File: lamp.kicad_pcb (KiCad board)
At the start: 2 copper layers, 24 x 24 mm, 39 parts, among them J101 Conn_01x01_Female, J102 Conn_01x01_Female, J103 Conn_01x01_Female, J104 Conn_01x01_Female, J105 Conn_01x01_Female, J106 Conn_01x01_Female, J107 Conn_01x01_Female, U101 STM32F030F4Px, U102 MIC5205-3.3, U103 TPS54620, U104 LMV321

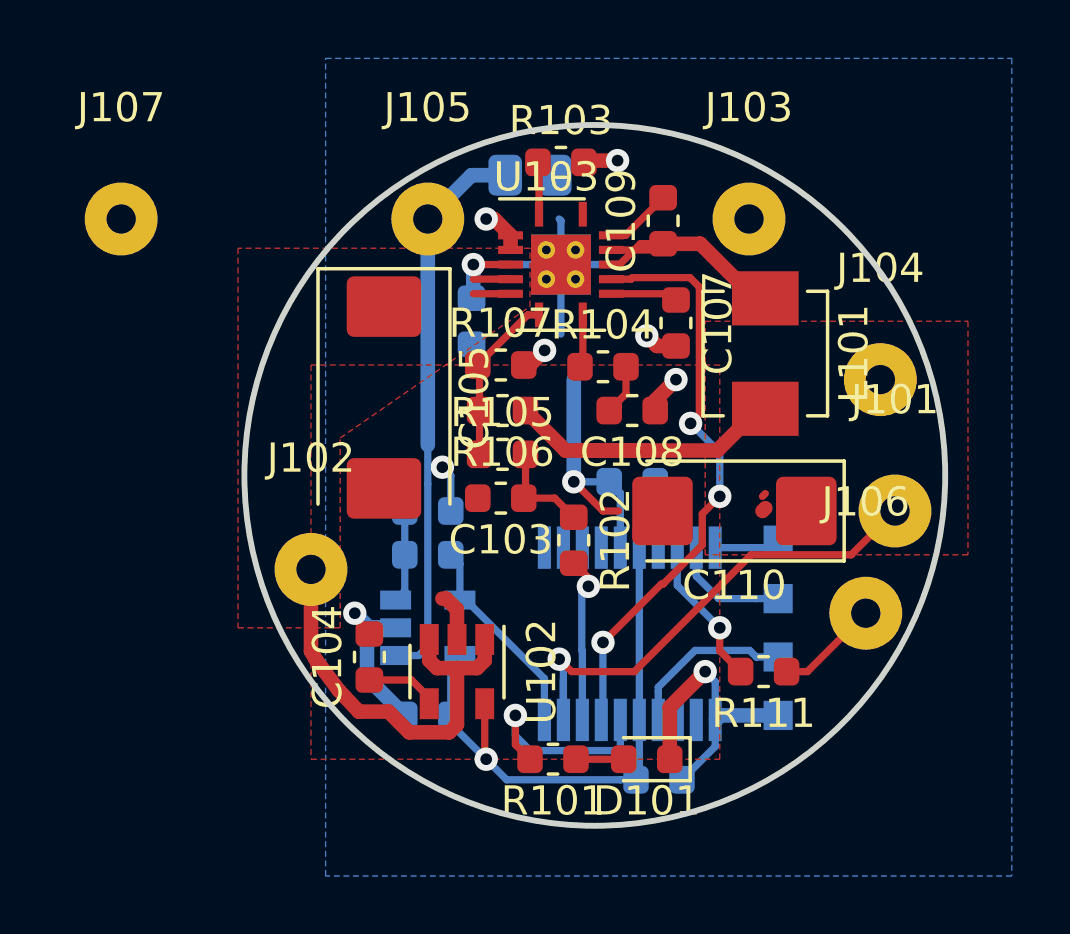
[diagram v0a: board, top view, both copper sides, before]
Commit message: Move to four layers, value selection
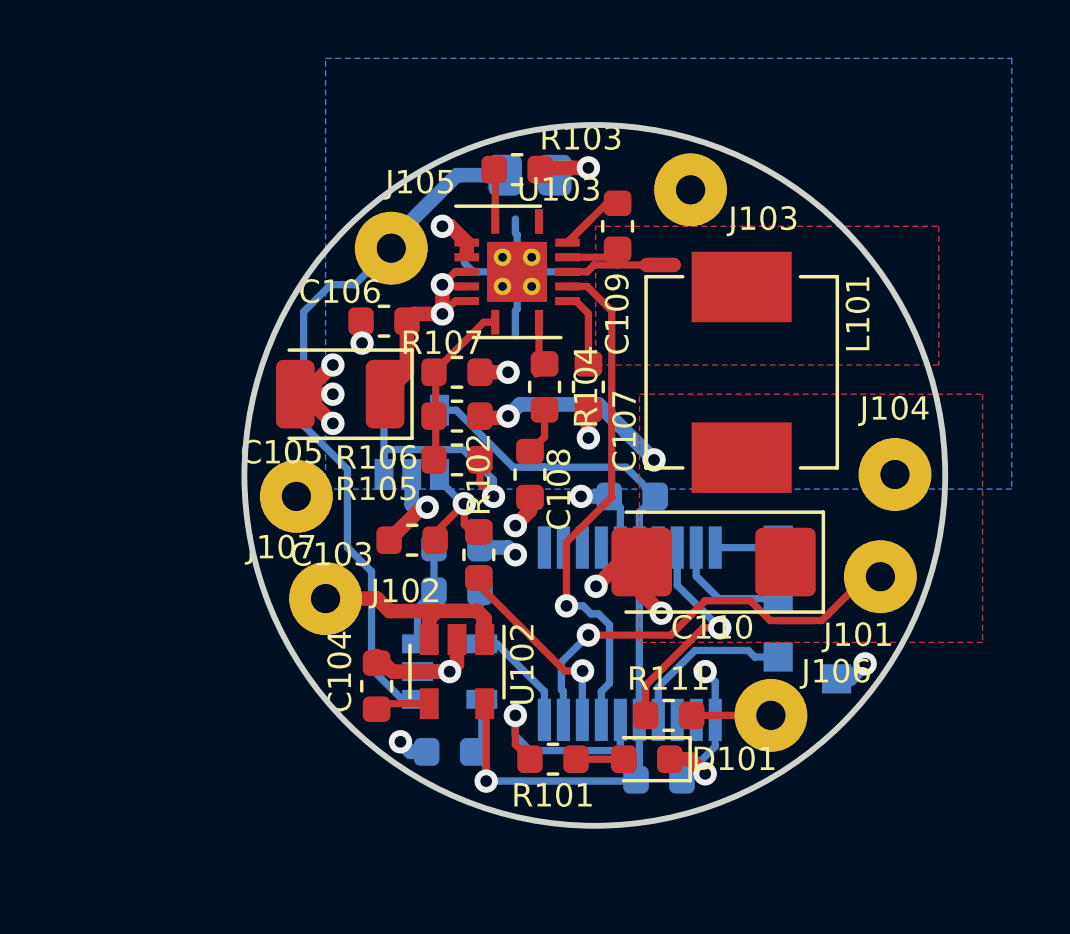
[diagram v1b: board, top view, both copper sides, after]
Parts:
- added U105: LMV321, Package_TO_SOT_SMD:SOT-23-5, B.Cu at (129.4, 82.7)
- C105: footprint Capacitor_Tantalum_SMD:CP_EIA-7343-31_Kemet-D -> Capacitor_Tantalum_SMD:CP_EIA-3528-12_Kemet-T
- C106: moved to F.Cu
- L101: value 3.3u -> 4.7u; footprint Inductor_SMD:L_Vishay_IHLP-1616 -> Inductor_SMD:L_Vishay_IHLP-2525
- R103: value R -> 40k
- R105: value R -> 50k
- R106: value R -> 22k
- R107: value R -> 4.7k
- moved J107 11.2 mm to (125.5, 84.5)
- moved J106 4.78 mm to (141.8, 92.0)
- moved C108 4.13 mm to (133.5, 83.8), turned to 90 degrees
- moved C107 3.71 mm to (135.5, 80.8)
- moved R111 3.58 mm to (138.2, 92.0)
- moved C103 3.36 mm to (129.5, 86.0)
- moved J104 3.29 mm to (146.0, 83.8)
- moved R102 3.29 mm to (131.8, 86.5)
- moved C106 3.00 mm to (128.5, 78.5), turned to 180 degrees
- moved TP104 2.36 mm to (144.0, 90.8)
- moved J101 2.30 mm to (145.5, 87.2)
- moved J103 2.24 mm to (139.0, 74.0)
- moved R104 2.12 mm to (134.0, 80.8), turned to 270 degrees
- moved C110 1.89 mm to (139.8, 86.8)
- moved U104 1.68 mm to (130.8, 90.5)
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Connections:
- R105 pad 2: /SETPOINT -> Net-(R105-Pad2)
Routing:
- net Net-(R105-Pad2): track 0.00 -> 9.20 mm, vias 0 -> 1
- net +3V3: track 22.0 -> 30.2 mm
- net /LED_P: track 12.1 -> 6.88 mm, vias 0 -> 2
- net /ISENSE: track 19.1 -> 24.2 mm
- net /VIN: track 20.3 -> 15.8 mm, vias 1 -> 2
- net /LED2: track 5.14 -> 7.73 mm
- net /EN: track 20.2 -> 17.7 mm, vias 3 -> 1
- net /SW: track 8.42 -> 6.38 mm
- net GND: track 42.3 -> 44.0 mm, vias 9 -> 19
- net Net-(C109-Pad2): track 2.31 -> 3.42 mm
- net /SETPOINT: track 3.48 -> 4.51 mm, vias 0 -> 1
- net Net-(R109-Pad2): track 7.10 -> 6.11 mm
- net /BTN: track 17.5 -> 16.5 mm
- net Net-(J106-Pad1): track 3.54 -> 2.71 mm
- net Net-(R102-Pad2): track 5.68 -> 6.45 mm
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- added copper zone on F.Cu, net /SW
- added copper zone on In2.Cu, net /VIN
- added copper zone on In1.Cu, net GND
- removed copper zone on F.Cu, net /VIN
- removed copper zone on F.Cu, net GND
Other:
- copper layers 2 -> 4

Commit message: More iteration
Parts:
- added C112: 100n, Capacitor_SMD:C_0603_1608Metric, B.Cu at (131.8, 86.0)
- added C113: 100n, Capacitor_SMD:C_0603_1608Metric, B.Cu at (133.0, 82.8)
- added C114: 100n, Capacitor_SMD:C_0603_1608Metric, F.Cu at (133.8, 88.8)
- C108: value 8.2n -> 22n
- C110: footprint Capacitor_Tantalum_SMD:CP_EIA-6032-28_Kemet-C -> Capacitor_Tantalum_SMD:CP_EIA-7343-15_Kemet-W
- L101: footprint Inductor_SMD:L_Vishay_IHLP-2525 -> Inductor_SMD:L_7.3x7.3_H4.5
- R104: value 1.8k -> 1k
- moved J102 3.64 mm to (125.5, 84.5)
- moved J107 3.58 mm to (126.2, 88.0)
- moved TP104 2.06 mm to (143.5, 88.8)
- moved R110 1.53 mm to (129.5, 86.7), turned to 270 degrees
- moved TP101 1.27 mm to (141.8, 88.8)
- moved TP102 1.03 mm to (141.8, 87.0)
- moved C109 1.00 mm to (136.5, 74.2)
- moved C108 0.90 mm to (134.2, 83.2), turned to 180 degrees
- moved TP103 0.79 mm to (141.8, 85.2)
- moved R109 0.75 mm to (131.8, 87.8)
- moved C110 0.59 mm to (139.2, 87.0)
- moved L101 0.50 mm to (140.2, 80.2)
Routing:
- net GND: track 44.0 -> 50.5 mm, vias 19 -> 23
- net Net-(R105-Pad2): track 9.20 -> 12.3 mm
- net /BTN: track 16.5 -> 14.0 mm
- net /EN: track 17.7 -> 20.0 mm
- net Net-(C112-Pad1): track 3.83 -> 5.62 mm
- net Net-(C112-Pad2): track 6.11 -> 7.54 mm
- net /LED2: track 7.73 -> 6.34 mm
- net /SETPOINT: track 4.51 -> 5.06 mm
- net /VIN: track 15.8 -> 15.4 mm, vias 2 -> 3
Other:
- board text added: "BTN"
- board text added: "GND"
- board text added: "IND"
- board text added: "OUT+"
- board text added: "OUT-"
- board text added: "VIN"

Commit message: More iteration
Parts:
- removed C101: 100n, Capacitor_SMD:C_0603_1608Metric
- added C1: 100n, Capacitor_SMD:C_0603_1608Metric, B.Cu at (137.8, 94.5)
- added C15: 100n, Capacitor_SMD:C_0603_1608Metric, F.Cu at (137.0, 93.0)
- added C16: 100n, Capacitor_SMD:C_0603_1608Metric, B.Cu at (133.5, 84.5)
- added R1: 90k, Resistor_SMD:R_0603_1608Metric, F.Cu at (134.2, 92.2)
- added R2: 10k, Resistor_SMD:R_0603_1608Metric, F.Cu at (137.0, 91.5)
- moved TP4 12.0 mm to (135.2, 80.0)
- moved R10 1.80 mm to (139.8, 91.0), turned to 90 degrees
- moved R3 1.04 mm to (134.0, 94.5)
- moved D1 1.02 mm to (137.7, 94.5)
- moved J4 0.90 mm to (142.5, 91.5)
- moved J6 0.50 mm to (146.0, 83.2)
- moved TP1 0.50 mm to (141.8, 89.2)
- moved C3 0.29 mm to (129.8, 86.0)
- moved R4 0.25 mm to (132.0, 86.5)
- moved TP2 0.25 mm to (141.8, 87.2)
- renumbered C107 to C10, C113 to C11, C108 to C12, C109 to C13, C110 to C14, C102 to C2, C103 to C3, C114 to C4, C111 to C5, C112 to C6, C104 to C7, C105 to C8, C106 to C9, D101 to D1, J102 to J1, J103 to J2, J101 to J3, J106 to J4, J107 to J5, J104 to J6, J105 to J7, L101 to L1, R111 to R10, R106 to R11, R107 to R12, R108 to R13, R101 to R3, R102 to R4, R109 to R5, R110 to R6, R103 to R7, R104 to R8, R105 to R9, TP101 to TP1, TP102 to TP2, TP103 to TP3, TP104 to TP4, U101 to U1, U104 to U2, U102 to U3, U103 to U4, U105 to U5
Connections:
- U1 pad 14: Net-(U101-Pad14) -> /VBAT
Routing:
- net /VBAT: track 0.00 -> 9.26 mm, vias 0 -> 1
- net GND: track 50.5 -> 58.3 mm, vias 23 -> 25
- net +3V3: track 29.8 -> 35.2 mm
- net /VIN: track 15.4 -> 19.3 mm
- net Net-(R9-Pad2): track 12.3 -> 8.67 mm
- net /EN: track 20.0 -> 17.4 mm, vias 1 -> 2
- net Net-(C16-Pad1): track 7.54 -> 9.21 mm
- net /LED2: track 6.34 -> 4.71 mm
- net /BTN: track 14.0 -> 15.6 mm
- net /SETPOINT: track 5.06 -> 4.05 mm
- net /LED1: track 7.21 -> 7.99 mm
- net Net-(D1-Pad2): track 1.64 -> 2.18 mm
- net /LED_P: track 6.76 -> 7.28 mm, vias 2 -> 0
- added copper zone on F.Cu, net GND

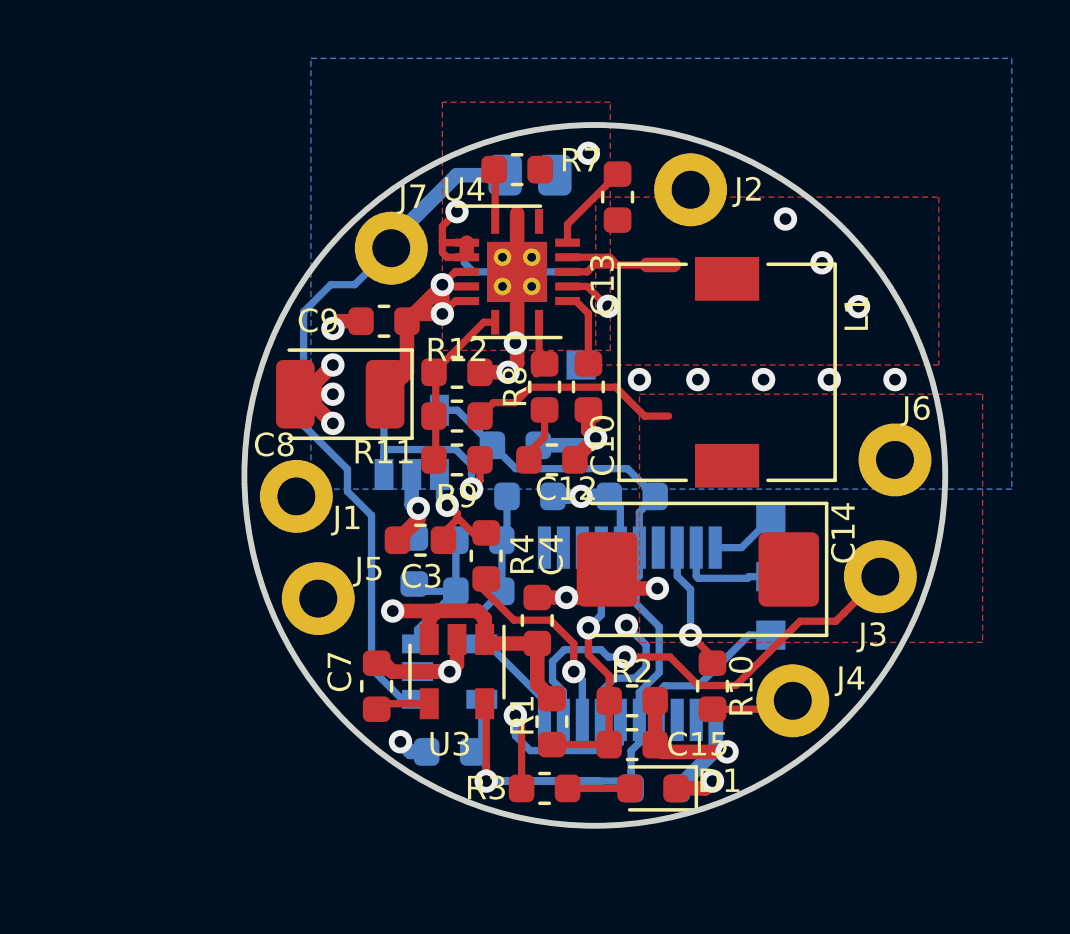
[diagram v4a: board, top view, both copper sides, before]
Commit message: Make LED PWMable
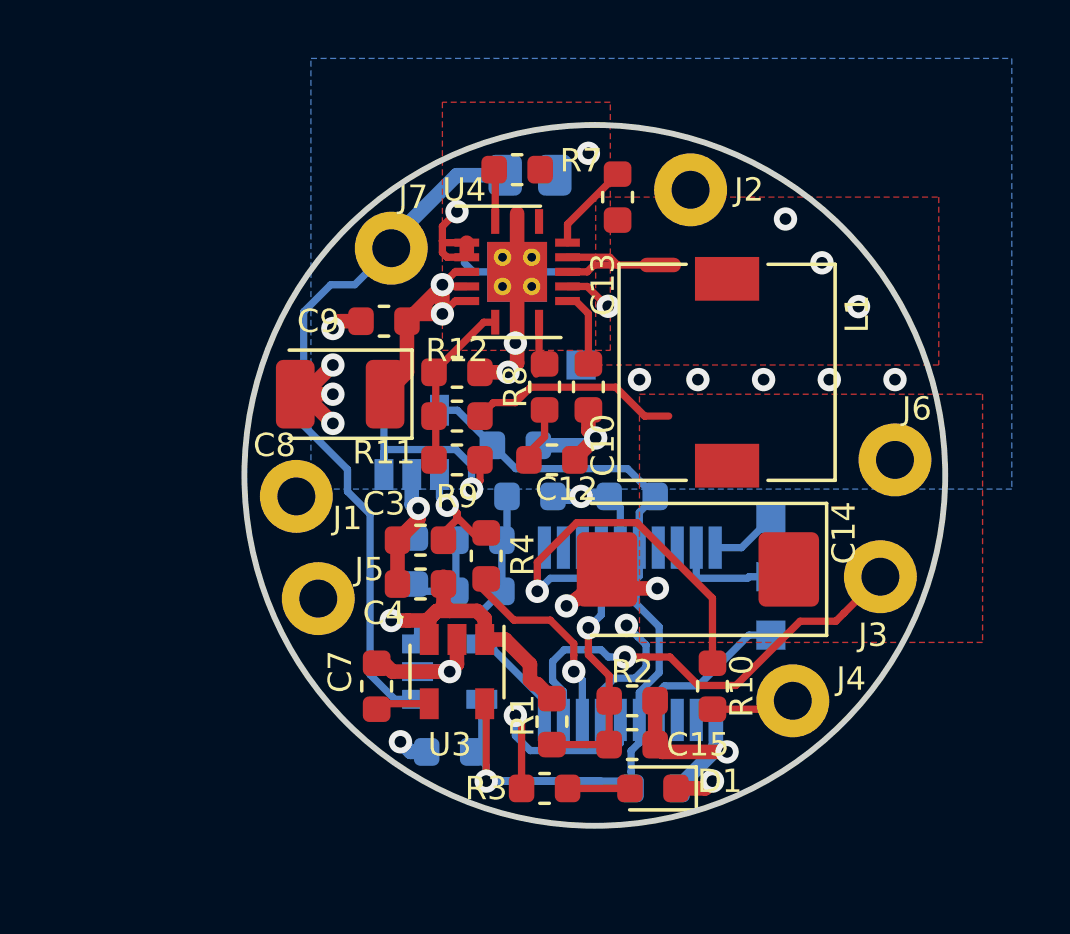
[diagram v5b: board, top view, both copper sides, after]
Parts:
- C15, C16: value 100n -> 10n
- R1: value 90k -> 47k
- R5: value 1k -> 100k
- U1: value STM32F030F4Px -> STM32F030F4P6
- moved C4 4.19 mm to (129.8, 87.5), turned to 180 degrees
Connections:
- U1 pad 13: Net-(U1-Pad13) -> /LED2
- U1 pad 18: /LED2 -> Net-(U1-Pad18)
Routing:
- net /LED2: track 4.71 -> 13.6 mm
- net /VIN: track 19.3 -> 20.2 mm

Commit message: Make other LED PWMable
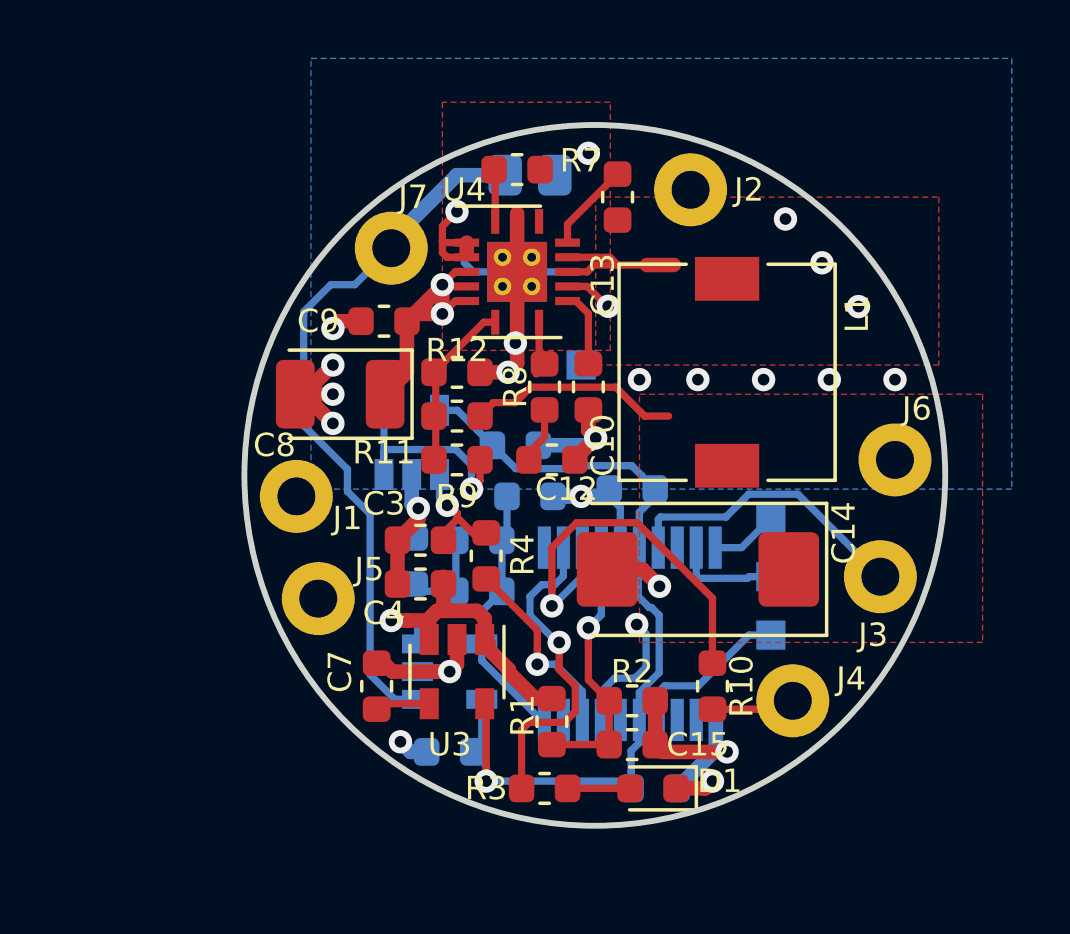
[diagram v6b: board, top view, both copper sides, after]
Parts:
- moved C2 0.25 mm to (137.0, 84.2)
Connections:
- U1 pad 12: Net-(U1-Pad12) -> /LED1
- U1 pad 17: Net-(U1-Pad17) -> /BTN
- U1 pad 6: /LED1 -> Net-(U1-Pad6)
- U1 pad 9: /BTN -> Net-(U1-Pad9)
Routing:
- net /BTN: track 15.6 -> 10.1 mm, vias 1 -> 0
- net +3V3: track 35.2 -> 31.2 mm
- net /LED1: track 7.99 -> 11.1 mm
- net GND: track 58.6 -> 57.6 mm, vias 25 -> 24

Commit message: Wibbles
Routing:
- net GND: track 57.6 -> 59.4 mm, vias 24 -> 25
- net /EN: track 17.4 -> 16.8 mm

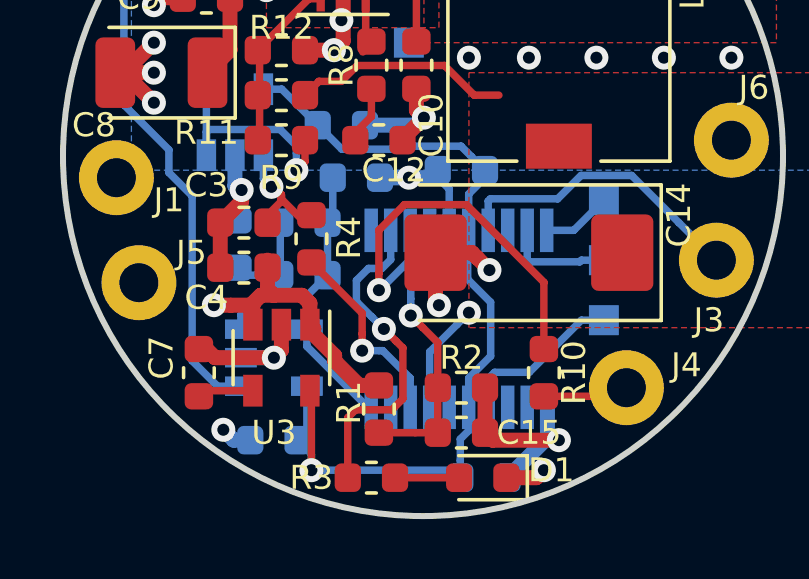
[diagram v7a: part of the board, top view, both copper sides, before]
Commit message: Use timers that are available on all parts
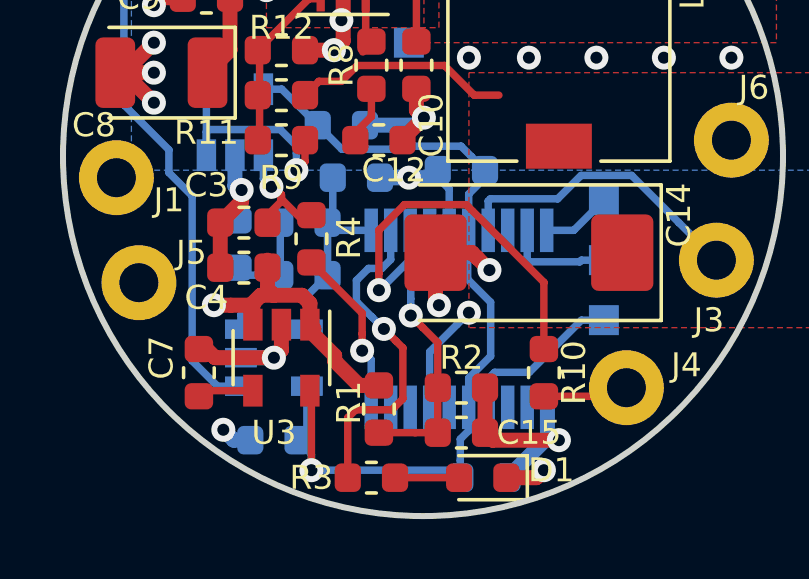
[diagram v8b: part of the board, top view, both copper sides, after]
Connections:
- U1 pad 10: Net-(C16-Pad1) -> Net-(R4-Pad2)
- U1 pad 11: Net-(U1-Pad11) -> Net-(C16-Pad1)
- U1 pad 8: Net-(R4-Pad2) -> Net-(U1-Pad8)
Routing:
- net Net-(C16-Pad1): track 9.05 -> 7.06 mm
- net Net-(R4-Pad2): track 6.63 -> 5.81 mm
